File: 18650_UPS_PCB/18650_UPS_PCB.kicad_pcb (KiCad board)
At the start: 4 copper layers, 90 x 22 mm, 54 parts, among them J1 USB_B_Micro, J2 Conn_02x04_Odd_Even, J3 USB_A, SW1 SW_SPDT, SW2 ALPSALPINE_SKRHADE011, SW3 SW_SPDT, SW4 SW_SPDT, SW5 SW_SPDT, U1 STLINK-V3MINI, U10 LR9102G-xx, U2 R5478, U3 STC4054, U4 FS8205A, U5 ME2188Cxx, U6 XC9236Axx, U7 INA219AxD, U8 SSD1306_128_32, U9 STM32F030F4Px

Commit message: routing
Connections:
- R6 pad 1: PA0 -> PA1
- R7 pad 1: PA1 -> PA0
- SW3 pad 1: PA0 -> PA1
- SW4 pad 1: PA1 -> PA0
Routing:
- net Shunt-: track 38.4 -> 190.8 mm, vias 0 -> 11
- net -BATT: track 27.6 -> 143.4 mm, vias 0 -> 6
- net +3.3VA: track 35.4 -> 99.6 mm, vias 0 -> 5
- net +5V: track 7.37 -> 68.2 mm, vias 0 -> 6
- net I2C1_SDA: track 2.11 -> 51.4 mm, vias 0 -> 3
- net I2C1_SCL: track 2.15 -> 47.6 mm, vias 0 -> 3
- net GNDD: track 72.6 -> 116.4 mm, vias 0 -> 17
- net LDOCE: track 0.00 -> 36.4 mm, vias 0 -> 2
- net PA7: track 0.00 -> 26.8 mm, vias 0 -> 2
- net PA1: track 0.00 -> 26.8 mm, vias 0 -> 2
- net USART1_RX: track 0.00 -> 21.0 mm, vias 0 -> 2
- net Net-(BT1-Pad1): track 4.60 -> 25.2 mm, vias 0 -> 3
- net NRST: track 4.38 -> 22.9 mm
- net PA0: track 0.00 -> 18.2 mm, vias 0 -> 2
- net USART1_TX: track 0.00 -> 15.7 mm, vias 0 -> 2
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
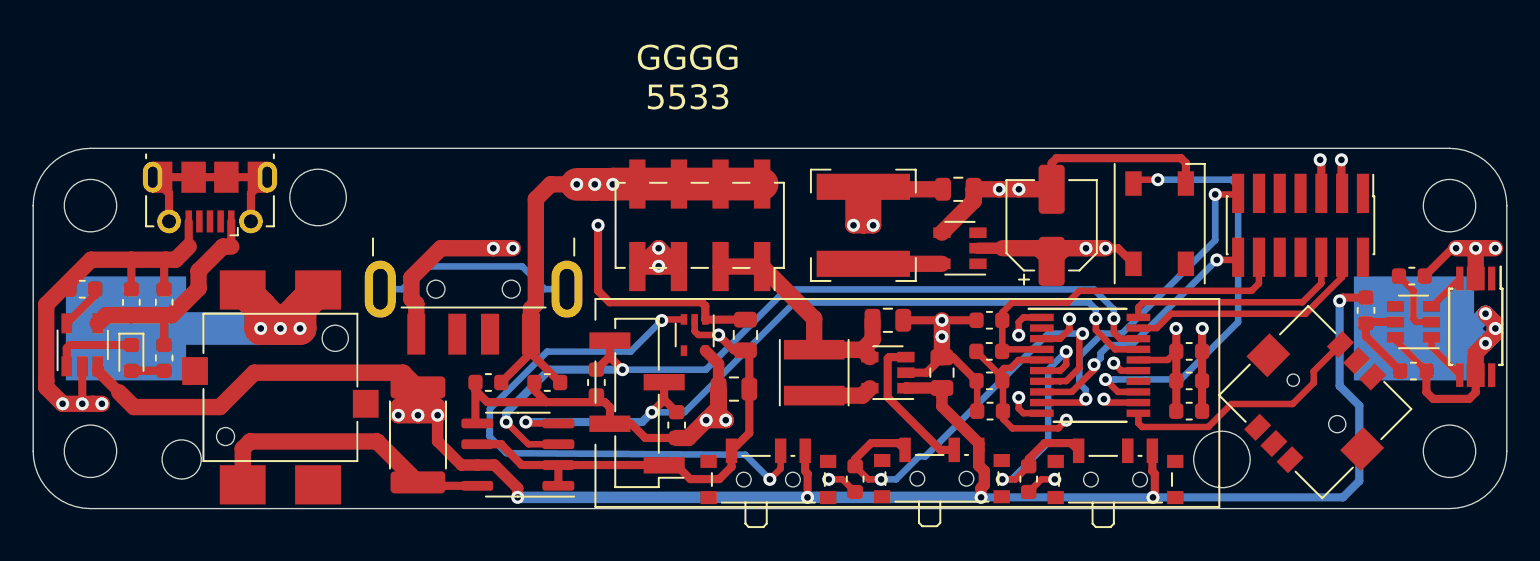
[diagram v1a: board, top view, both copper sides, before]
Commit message: 1 net left
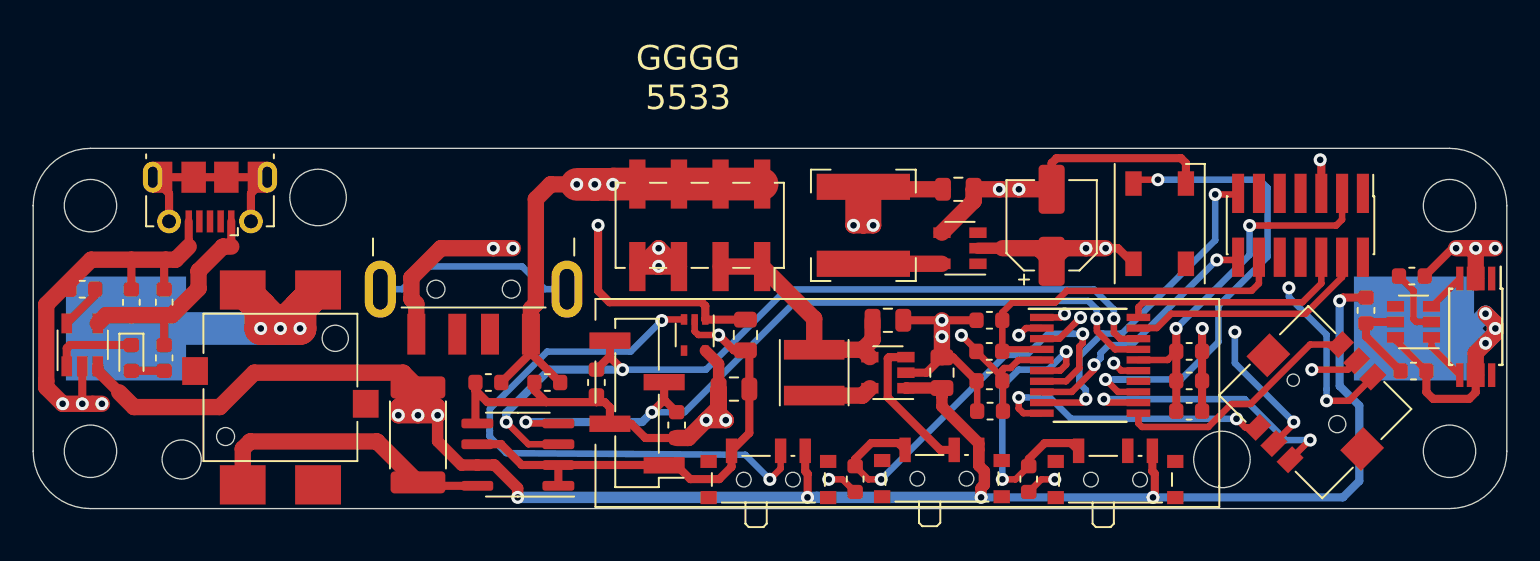
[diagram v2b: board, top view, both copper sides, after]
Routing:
- net PF0: track 0.00 -> 30.7 mm, vias 0 -> 3
- net PF1: track 2.57 -> 23.2 mm, vias 1 -> 3
- net PA6: track 2.20 -> 17.6 mm, vias 1 -> 2
- net PA4: track 2.20 -> 17.6 mm, vias 1 -> 2
- net PA7: track 26.8 -> 31.2 mm
- net GNDD: track 116.4 -> 118.5 mm, vias 17 -> 18
- net +3.3VA: track 99.6 -> 100.5 mm
- net PA0: track 18.2 -> 19.0 mm

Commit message: routing done
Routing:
- net BoostCE: track 0.00 -> 17.2 mm, vias 0 -> 2
- net PA0: track 19.0 -> 10.4 mm, vias 2 -> 0
- net PA7: track 31.2 -> 28.7 mm
- net PA6: track 17.6 -> 16.7 mm
- net USART1_RX: track 21.0 -> 21.6 mm
- net I2C1_SDA: track 51.4 -> 51.9 mm

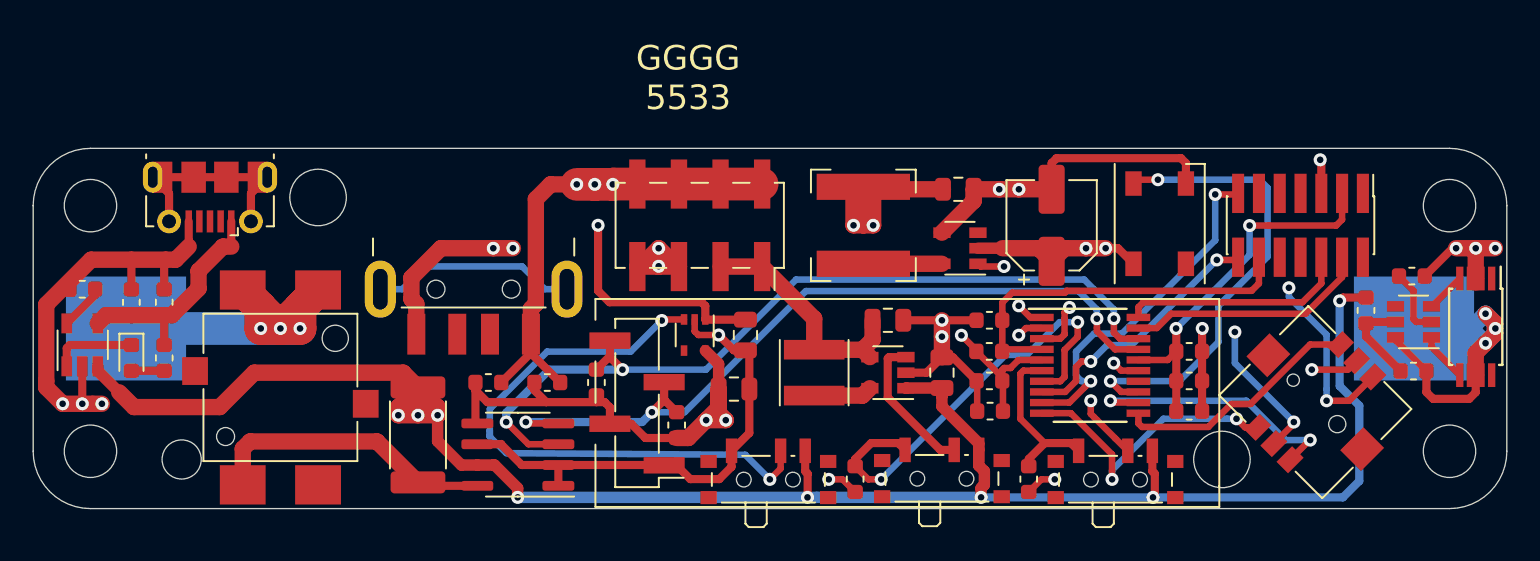
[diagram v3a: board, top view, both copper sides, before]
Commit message: routing cleanup
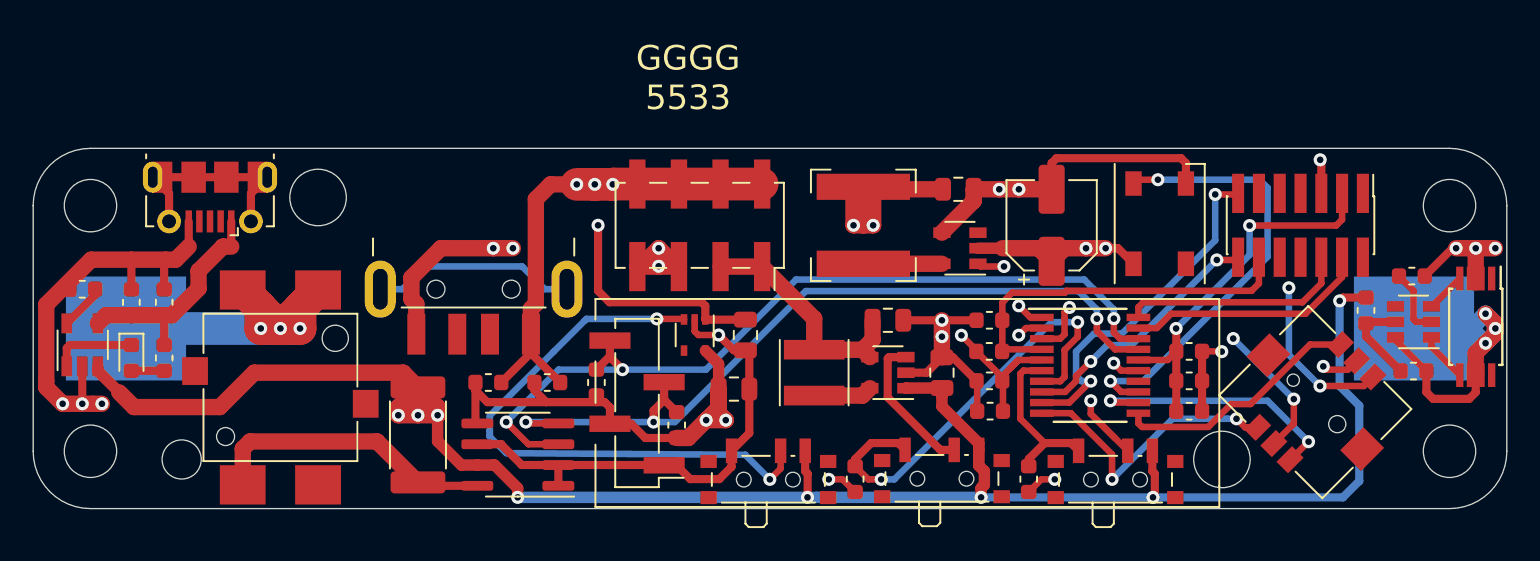
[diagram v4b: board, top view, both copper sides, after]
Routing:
- net BoostCE: track 17.2 -> 18.8 mm
- net PA7: track 28.7 -> 27.4 mm
- net PF0: track 30.7 -> 29.6 mm
- net GNDD: track 118.7 -> 117.9 mm
- net I2C1_SCL: track 48.2 -> 48.8 mm

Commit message: cleaned routing significantly
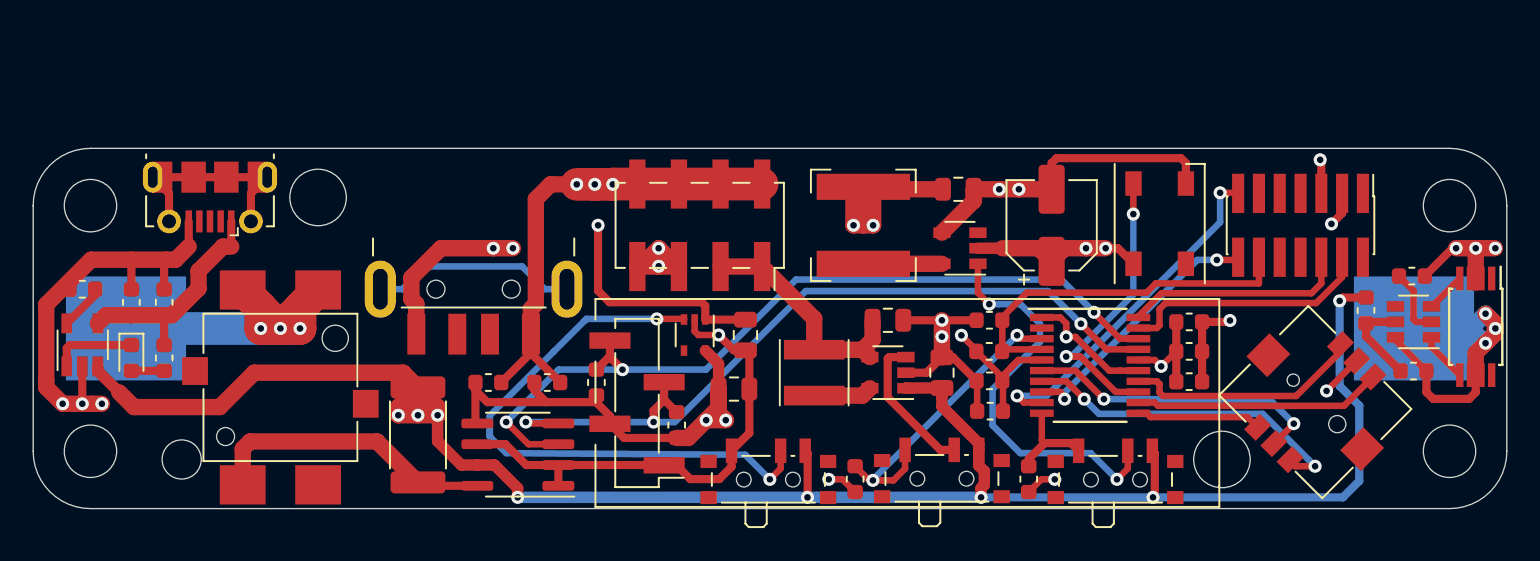
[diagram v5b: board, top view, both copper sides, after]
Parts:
- moved C16 1.80 mm to (191.4, 86.6)
- moved C15 1.80 mm to (191.4, 88.4)
- moved C17 1.80 mm to (191.4, 84.8)
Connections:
- R6 pad 1: PA1 -> PF1
- R7 pad 1: PA0 -> PA4
- SW2 pad 1: PA4 -> PA5
- SW2 pad 2: PF1 -> PA0
- SW2 pad 3: PA6 -> PA1
- SW2 pad 4: PA5 -> PB1
- SW2 pad 6: PF0 -> PA6
- SW3 pad 1: PA1 -> PF1
- SW4 pad 1: PA0 -> PA4
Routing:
- net PF0: track 29.6 -> 0.00 mm, vias 3 -> 0
- net PB1: track 0.00 -> 14.6 mm
- net PA4: track 17.6 -> 5.98 mm, vias 2 -> 0
- net PA7: track 27.4 -> 17.7 mm
- net PA0: track 10.4 -> 18.5 mm, vias 0 -> 2
- net PA5: track 15.1 -> 7.64 mm
- net PA1: track 27.1 -> 20.6 mm
- net BoostCE: track 18.8 -> 24.7 mm
- net GNDD: track 117.9 -> 123.0 mm, vias 18 -> 17
- net PF1: track 22.8 -> 19.0 mm, vias 3 -> 2
- net +3.3VA: track 101.0 -> 97.5 mm
- net PA6: track 16.5 -> 15.1 mm, vias 2 -> 0
- net I2C1_SDA: track 51.5 -> 50.7 mm
- net I2C1_SCL: track 48.8 -> 48.0 mm
- net SWDIO: track 14.9 -> 15.5 mm
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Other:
- board text removed: "GGGG 5533"
